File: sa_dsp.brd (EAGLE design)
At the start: 150 x 110 mm, 288 parts, among them CN1 uSD, CN3 2X5 HEADER, Q3 2N7002, Q4 2N7002, U1 PGA2311, U10 LME49720, U11 PGA2311, U12 LME49720, U13 LME49720, U14 PCM1754, U15 LME49720, U16 PGA2311, U17 LME49720, U18 LME49720, U19 PCM1754, U20 LME49720, U21 7 SEG, U22 74HC164A, U23 PCM2707, U24 PCM2707, U25 7 SEG, U26 74HC164A, U29 7 SEG, U3 OSD3358-512M-BSM, U30 74HC164A, U4 LME49720, U5 LME49720, U6 10CL016YF484C6G, U7 7 SEG, U8 74HC164A, U9 PCM1754

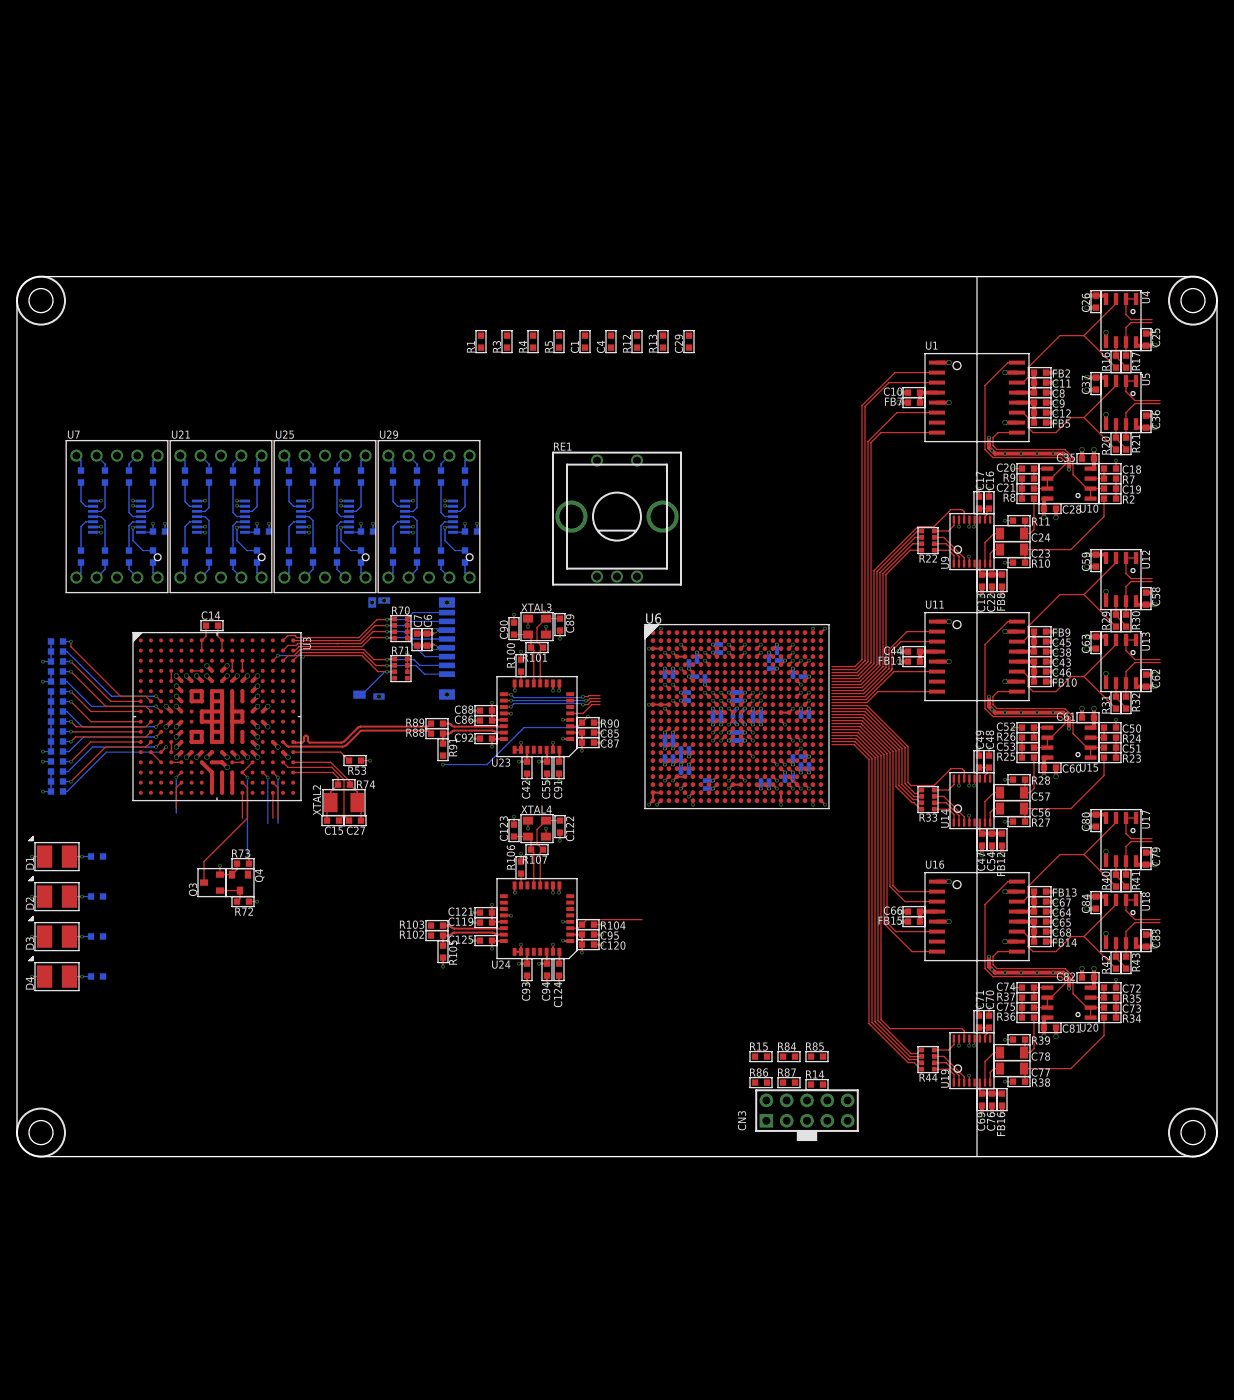
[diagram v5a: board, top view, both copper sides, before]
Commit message: Routing the anallogue section
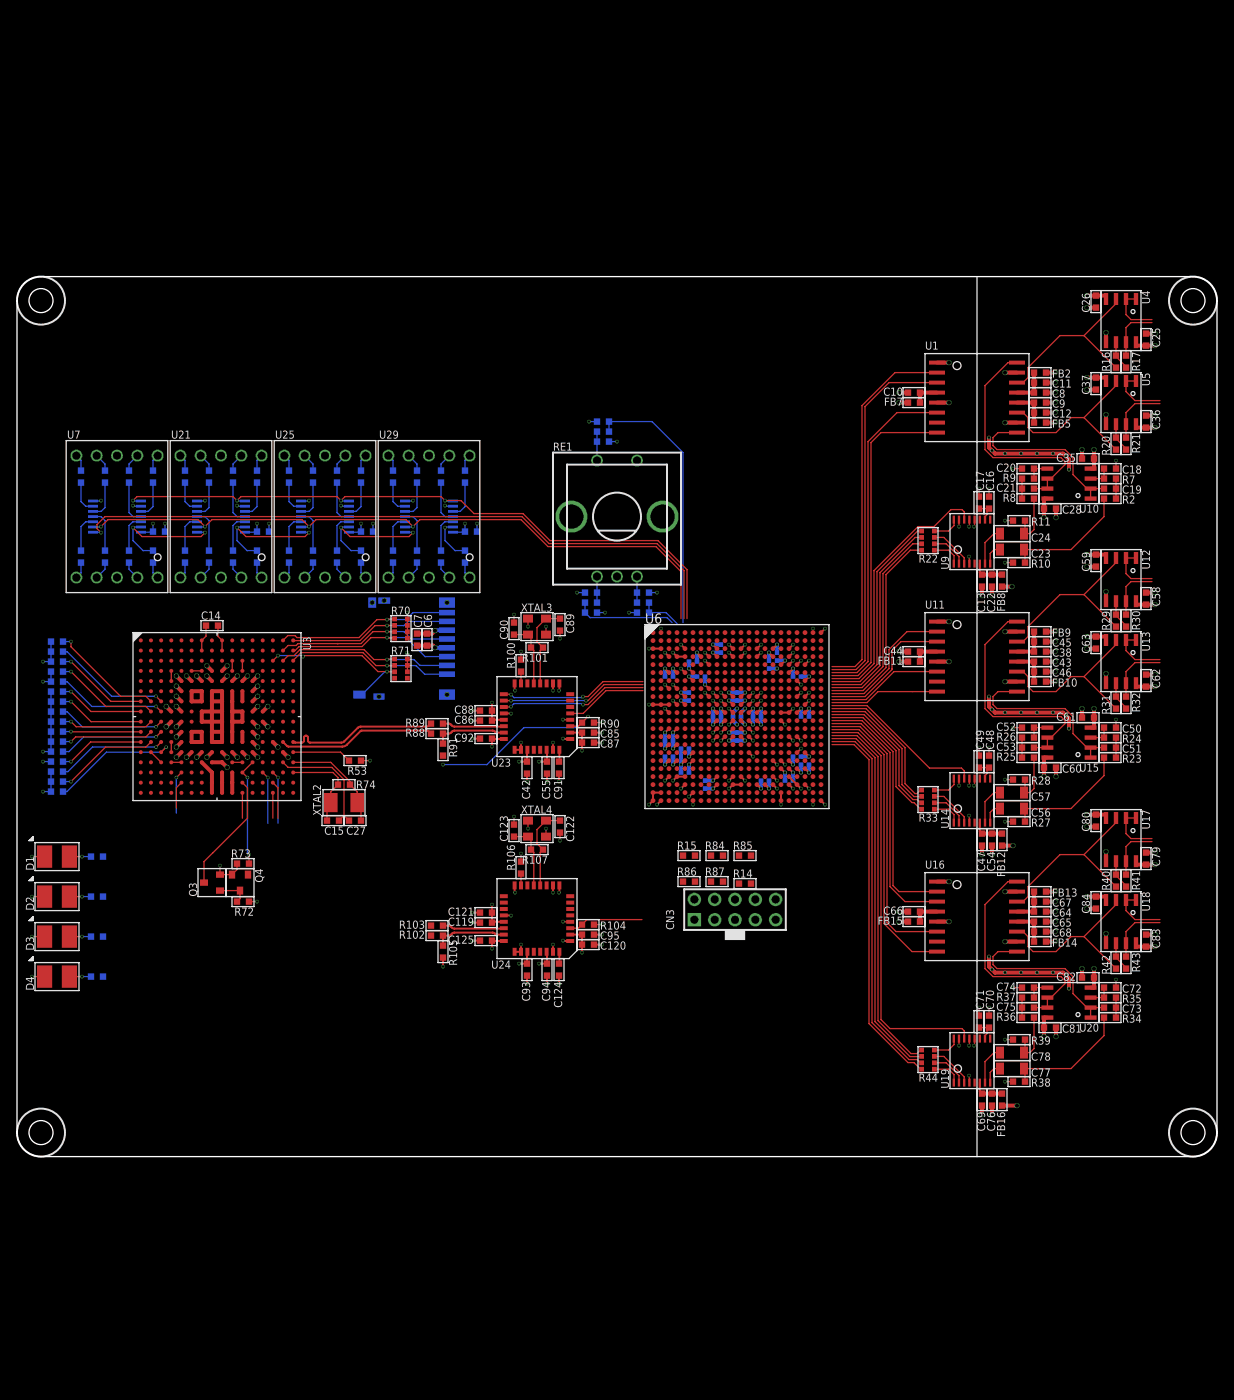
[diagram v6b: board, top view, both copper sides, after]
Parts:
- moved R3 35.7 mm to (78.2, 70.5), flipped to the bottom, turned to 180 degrees
- moved R5 34.3 mm to (78.2, 69.2), flipped to the bottom, turned to 180 degrees
- moved R1 34.3 mm to (71.8, 70.5), flipped to the bottom, turned to 0 degrees
- moved C4 34.1 mm to (78.2, 68.0), flipped to the bottom, turned to 180 degrees
- moved C1 33.9 mm to (71.8, 68.0), flipped to the bottom, turned to 0 degrees
- moved R4 33.4 mm to (71.8, 69.2), flipped to the bottom, turned to 0 degrees
- moved CN3 26.7 mm to (89.8, 30.9)
- moved R14 26.7 mm to (91.0, 34.1)
- moved R15 26.7 mm to (84.0, 37.6)
- moved R84 26.7 mm to (87.5, 37.6)
- moved R85 26.7 mm to (91.0, 37.6)
- moved R86 26.7 mm to (84.0, 34.4)
- moved R87 26.7 mm to (87.5, 34.4)
- moved C29 14.7 mm to (73.2, 91.9), flipped to the bottom, turned to 180 degrees
- moved R13 13.5 mm to (73.2, 90.6), flipped to the bottom, turned to 0 degrees
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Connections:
- new net DISP_SPI_MOSI1: R46.2, U22.1, U8.13
- new net DISP_SPI_MOSI2: R79.2, U22.13, U26.1
- new net DISP_SPI_MOSI3: R96.2, U26.13, U30.1
- net DISP_SPI_MOSI: no longer U22.1, U26.1, U30.1
- net SHIFT_OUT: no longer R46.2, R79.2, R96.2, U22.13, U26.13, U8.13
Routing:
- net +5V: track 31.7 -> 276.2 mm
- net -5V: track 28.3 -> 203.6 mm
- net DISP_SPI_!CE: track 4.08 -> 87.7 mm
- net DISP_SPI_MOSI: track 4.08 -> 84.8 mm, vias 4 -> 1
- net DISP_SPI_SCLK: track 4.08 -> 84.3 mm
- net ENC_SW: track 0.00 -> 33.4 mm
- net SHIFT_OUT: track 22.7 -> 5.67 mm, vias 4 -> 1
- net DISP_SPI_MOSI2: track 0.00 -> 16.4 mm, vias 0 -> 2
- net DISP_SPI_MOSI3: track 0.00 -> 16.4 mm, vias 0 -> 2
- net DISP_SPI_MOSI1: track 0.00 -> 16.4 mm, vias 0 -> 2
- net ENC_A: track 0.00 -> 12.6 mm
- net PCM_I2S_MCLK_BB: track 12.1 -> 18.2 mm
- net PCM_I2S_LRCLK_BB: track 4.18 -> 10.3 mm
- net PCM_I2S_BCLK_BB: track 12.4 -> 18.5 mm
- net PCM_I2S_DOUT_BB: track 12.3 -> 18.4 mm
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- added copper zone on layer 2, net AGND
- added copper zone on layer 3, net AGND

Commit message: General progress
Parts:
- added C126, C129, C130, C33, C34, C40: 100uF 50V, CAPACITORS:8MM_RADIAL_3.5MM_PITCH
- added C127, C128, C31, C32, C39, C41: 10nF 50V, CAPACITORS:0603
- added C131, C132: 100nF 16V, CAPACITORS:0603
- added D5, D6: RED STATUS, OPTO:VLMT3100
- added FB1, FB3, FB4: 600R, INDUCTORS:0603
- added L1, L2, L3: 47uH 0.9A, INDUCTORS:SRN5040
- added R116, R119, R120: 240R, r_0603:0603
- added R117, R118, R121: 750R, r_0603:0603
- added R122: 10k, r_0603:0603
- added R123, R124, R125: 1.0k, r_0603:0603
- added SW1: 1825910-7, ELECTROMECH:TH_TACT_SWITCH
- added TP1, TP2: TEST_POINT_SQUARE, MISC:OSPREY_HSS_PAD
- added U2, U28: LM317, ICs:TO220
- added U27: LM337, ICs:TO220
- added U31: 100MHz, CRYSTALS:5X3.2SEAM
- CN3: value 2X5 HEADER -> 2X5_HEADER
- U23, U24: value PCM2707 -> (none)
- XTAL3, XTAL4: value 12MHz -> (none)
- moved CN3 21.9 mm to (70.4, 41.1)
- moved R14 21.9 mm to (71.6, 44.4), flipped to the bottom
- moved R86 21.9 mm to (64.6, 44.6), flipped to the bottom
- moved R87 21.9 mm to (68.1, 44.6), flipped to the bottom
- moved R85 17.9 mm to (74.6, 44.9), flipped to the bottom
- moved R84 16.5 mm to (74.1, 47.2), flipped to the bottom
- moved R15 16.0 mm to (70.6, 46.4), flipped to the bottom
- moved C119 14.9 mm to (44.2, 33.0)
- moved C120 14.9 mm to (57.0, 30.2)
- moved C121 14.9 mm to (44.2, 34.2)
- moved C124 14.9 mm to (53.4, 27.1)
- moved C125 14.9 mm to (44.2, 30.8)
- moved C93 14.9 mm to (49.4, 27.1)
- moved C94 14.9 mm to (51.9, 27.1)
- moved C95 14.9 mm to (57.0, 31.5)
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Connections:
- new net 15VA+_UNREG: L1.1
- new net 15VA-_UNREG: L2.1
- new net 15VD_UNREG: L3.1
- new net 5VD: R90.2, R91.2, U23.3, U3.M15, U3.P10, U3.R10, U3.T10
- new net CLK_100M: U31.3, U6.A11
- new net CLK_100M_OE: U31.1, U6.A10
- new net N$10: FB1.1, L1.2
- new net N$176: R120.1, R121.2, U28.1
- new net N$177: R118.1, R119.2, U27.1
- new net N$178: C127.2, C129.P, FB4.2, U28.3
- new net N$179: FB4.1, L3.2
- new net N$180: R122.1, R123.1, SW1.1, SW1.2
- new net N$181: D5.A, R124.2
- new net N$182: D6.A, R125.2
- new net N$3: R116.1, R117.2, U2.1
- new net N$4: C39.1, C40.N, FB3.2, U27.2
- new net N$6: C31.2, C33.P, FB1.2, U2.3
- new net N$7: FB3.1, L2.2
- new net UI_INPUT_AIRPLAY: R124.1
- new net UI_INPUT_SEL: C132.2, R123.2
- new net UI_INPUT_USB: R125.1
- net +5V: now also C32.2, C34.P, R116.2, U2.2
- net -5V: now also C126.N, C41.1, R119.1, U27.3
- net 3V3: now also C131.2, R122.2, U31.4
- net 5V: now also C128.2, C130.P, R120.2, U28.2; no longer R90.2, R91.2, U23.3, U3.M15, U3.P10, U3.R10, U3.T10
- net AGND: now also C126.P, C31.1, C32.1, C33.N, C34.N, C39.2, C40.P, C41.2, R117.1, R118.2, TP2.1
- net GND: now also C127.1, C128.1, C129.N, C130.N, C131.1, C132.1, D5.K, D6.K, R121.1, SW1.3, SW1.4, TP1.1, U31.2
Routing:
- net 5V: track 34.6 -> 131.6 mm, vias 9 -> 6
- net -5V: track 203.6 -> 259.7 mm, vias 12 -> 13
- net +5V: track 276.2 -> 324.3 mm
- net 5VD: track 0.00 -> 27.6 mm, vias 0 -> 3
- net N$4: track 0.00 -> 18.2 mm
- net N$178: track 0.00 -> 17.7 mm
- net N$6: track 0.00 -> 15.5 mm
- net GND: track 218.4 -> 227.7 mm, vias 186 -> 208
- net CLK_100M_OE: track 0.00 -> 7.34 mm
- net AGND: track 114.4 -> 120.9 mm, vias 90 -> 113
- net N$3: track 0.00 -> 4.62 mm
- net N$177: track 0.00 -> 4.62 mm
- net N$176: track 0.00 -> 4.62 mm
- net CLK_100M: track 0.00 -> 4.25 mm
- net N$19: track 10.8 -> 6.65 mm
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
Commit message: Libraies sorted
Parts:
- CN3: value 2X5_HEADER -> 2X5 HEADER
- U23, U24: value (none) -> PCM2707
- XTAL3, XTAL4: value (none) -> 12MHz
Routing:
- net GND: track 227.7 -> 224.2 mm
